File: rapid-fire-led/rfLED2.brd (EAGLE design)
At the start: 76.8 x 48.9 mm, 47 parts, among them IC1 REG

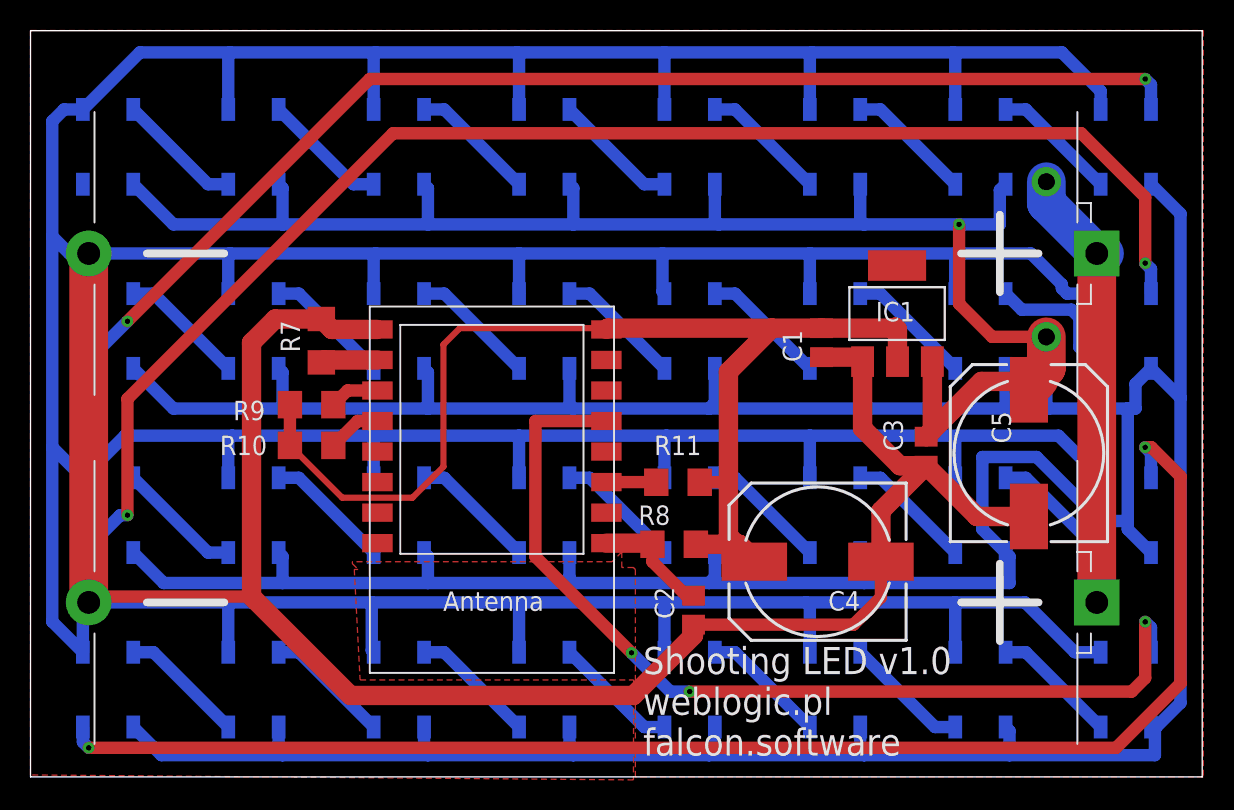
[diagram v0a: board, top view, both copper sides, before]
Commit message: adds capacitor to each WS2812 LED
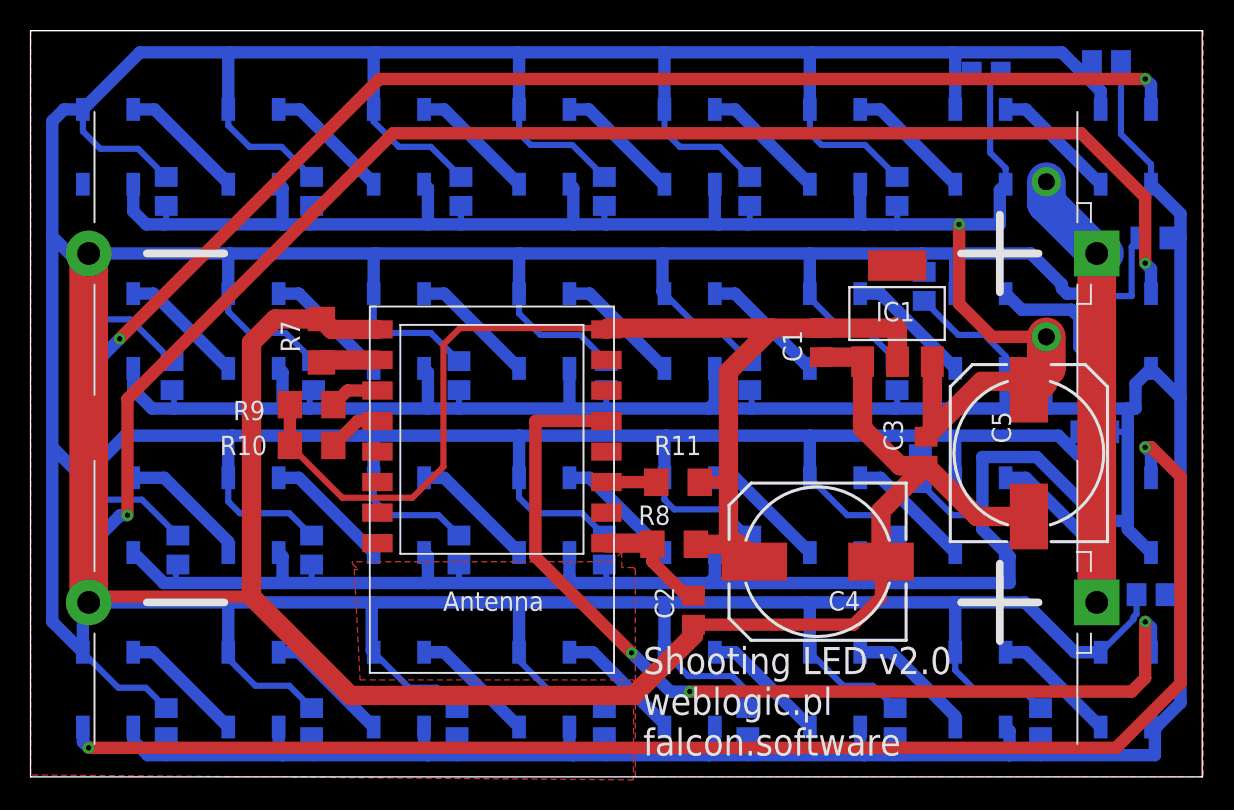
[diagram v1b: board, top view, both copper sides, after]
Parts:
- added C10, C11, C12, C13, C14, C15, C16, C17, C18, C19, C20, C21, C22, C23, C24, C25, C26, C27, C28, C29, C30, C31, C32, C33, C34, C35, C36, C37, C6, C7, C8, C9: (no value), eagle-ltspice:C0805
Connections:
- net GND: now also C10.2, C11.2, C12.2, C13.2, C14.2, C15.2, C16.2, C17.2, C18.2, C19.2, C20.2, C21.2, C22.2, C23.2, C24.2, C25.2, C26.2, C27.2, C28.2, C29.2, C30.2, C31.2, C32.2, C33.2, C34.2, C35.2, C36.2, C37.2, C6.2, C7.2, C8.2, C9.2
- net VCC: now also C10.1, C11.1, C12.1, C13.1, C14.1, C15.1, C16.1, C17.1, C18.1, C19.1, C20.1, C21.1, C22.1, C23.1, C24.1, C25.1, C26.1, C27.1, C28.1, C29.1, C30.1, C31.1, C32.1, C33.1, C34.1, C35.1, C36.1, C37.1, C6.1, C7.1, C8.1, C9.1
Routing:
- net GND: track 536.4 -> 748.9 mm
- net VCC: track 416.4 -> 482.0 mm
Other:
- board text added: "Shooting LED v2.0 weblogic.pl falcon.software"
- board text removed: "Shooting LED v1.0 weblogic.pl falcon.software"
